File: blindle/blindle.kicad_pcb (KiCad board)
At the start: 2 copper layers, 8 parts, among them J1 CONN_5V, J2 CONN_8V, M1 74HC595, P1 pololua4988, P2 pololua4988

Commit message: Actualizo la huella del pololu
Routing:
- net GNDD: track 78.9 -> 77.3 mm
- net +8V: track 65.2 -> 66.8 mm
- net +5V: track 223.3 -> 224.5 mm
- net Net-(P2-Pad14): track 14.8 -> 14.0 mm
- net Net-(P2-Pad13): track 14.8 -> 14.0 mm
- net Net-(P2-Pad12): track 14.8 -> 14.0 mm
- net Net-(P2-Pad11): track 14.8 -> 14.0 mm
- net Net-(P1-Pad14): track 14.1 -> 13.3 mm
- net Net-(P1-Pad13): track 14.1 -> 13.3 mm
- net Net-(P1-Pad12): track 14.1 -> 13.3 mm
- net Net-(P1-Pad11): track 14.1 -> 13.3 mm
- net GND: track 267.7 -> 266.9 mm

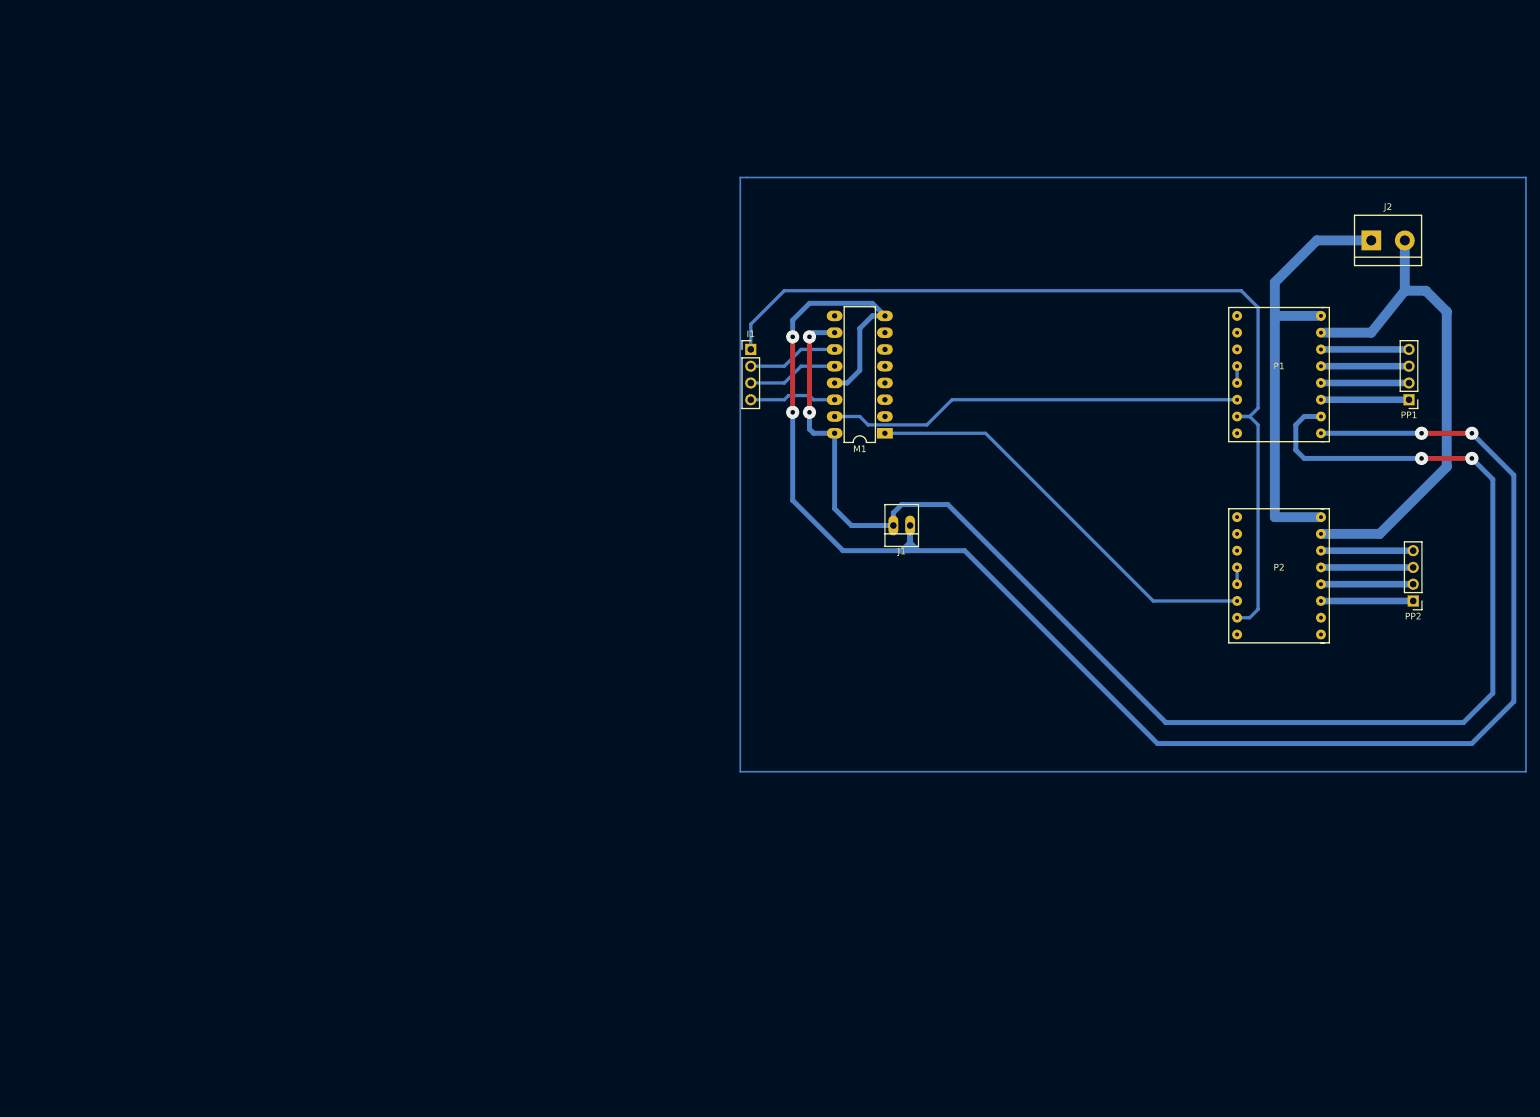
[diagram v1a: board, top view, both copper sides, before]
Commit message: Bug en plantilla pololu - Version 4 pololus
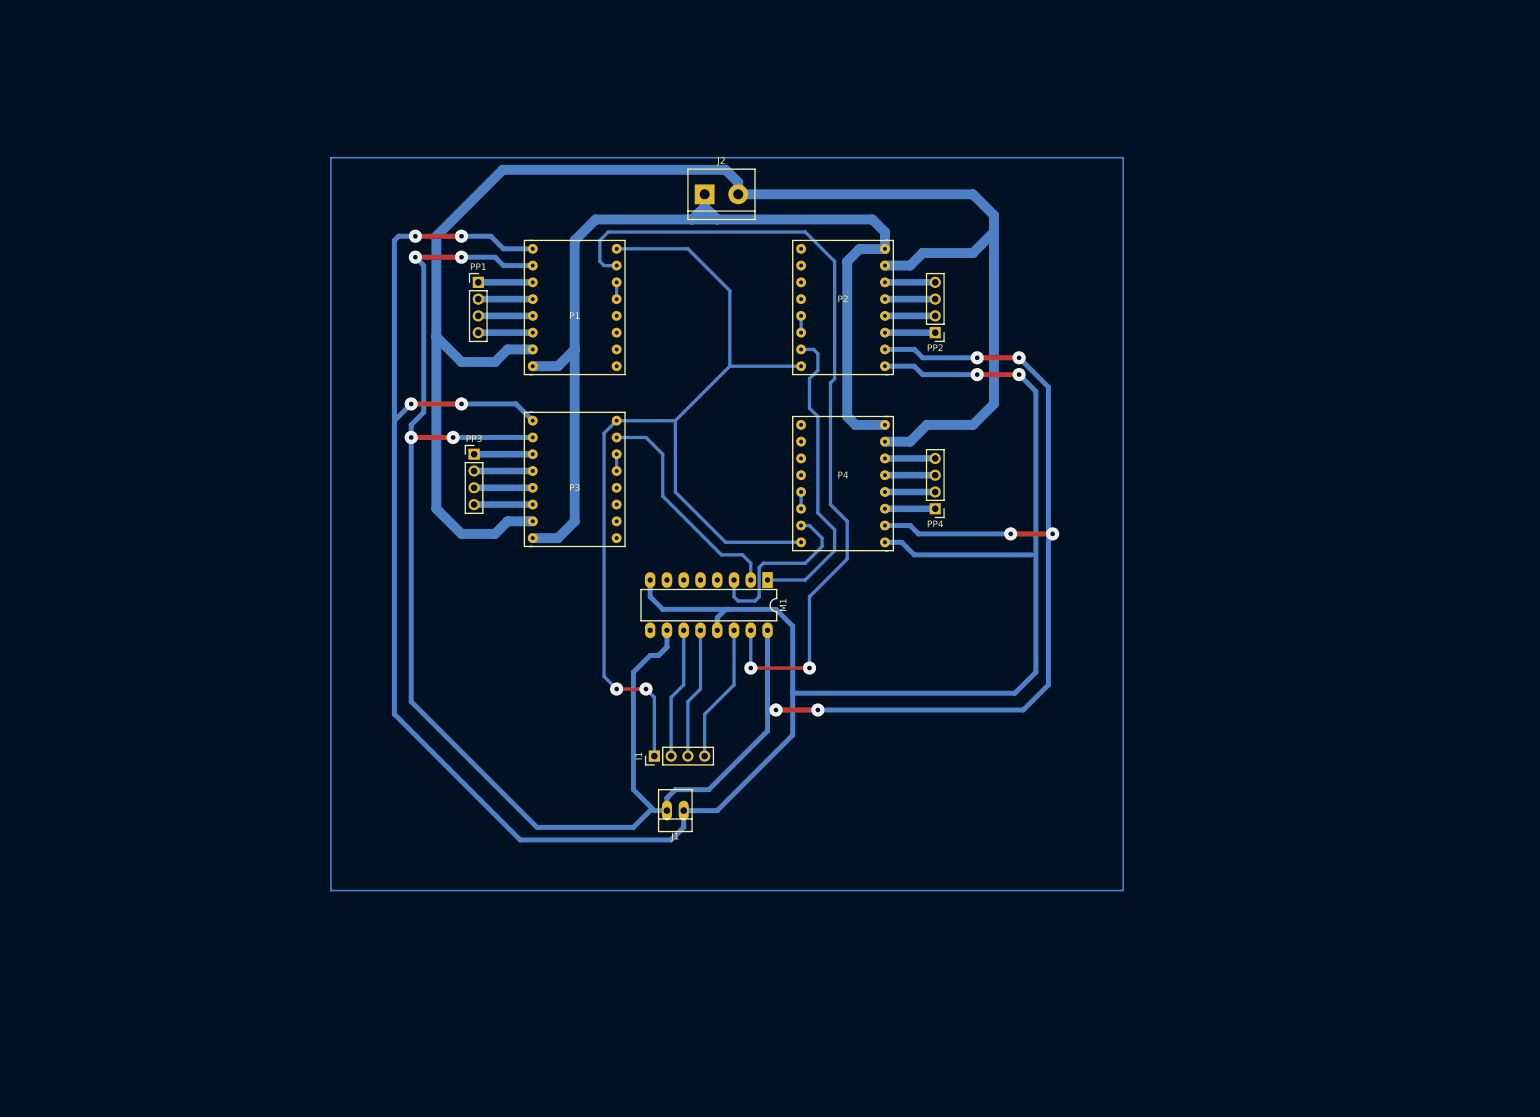
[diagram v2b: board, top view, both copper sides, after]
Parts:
- added P3: pololua4988, pololu:pololua4988, F.Cu at (128.3, 94.6)
- added P4: pololua4988, pololu:pololua4988, F.Cu at (156.2, 77.5)
- added PP3: CONN_MOTOR, Pin_Headers:Pin_Header_Straight_1x04_Pitch2.54mm, F.Cu at (106.7, 81.9)
- added PP4: CONN_MOTOR, Pin_Headers:Pin_Header_Straight_1x04_Pitch2.54mm, F.Cu at (176.5, 90.2)
- moved PP1 142.1 mm to (107.3, 55.9), turned to 0 degrees
- moved J2 101.2 mm to (141.6, 42.5)
- moved P1 94.3 mm to (128.3, 68.6), turned to 180 degrees
- moved PP2 83.0 mm to (176.5, 63.5)
- moved P2 77.5 mm to (156.2, 50.8)
- moved I1 63.3 mm to (134.0, 127.6), turned to 90 degrees
- moved J1 55.1 mm to (138.4, 135.9)
- moved M1 28.5 mm to (151.1, 101.0), turned to 270 degrees
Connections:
- I1 pad 1: Net-(I1-Pad1) -> dir
- P1 pad 4: sleep -> Net-(P1-Pad4)
- P1 pad 5: sleep -> Net-(P1-Pad5)
- P1 pad 6: Net-(M1-Pad15) -> Net-(P1-Pad5)
- P1 pad 7: Net-(I1-Pad1) -> Net-(M1-Pad15)
- P1 pad 8: (no net) -> dir
- P2 pad 5: Net-(P2-Pad4) -> Net-(P2-Pad5)
- P2 pad 6: Net-(M1-Pad1) -> Net-(P2-Pad5)
- P2 pad 7: Net-(I1-Pad1) -> Net-(M1-Pad1)
- P2 pad 8: (no net) -> dir
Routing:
- net GNDD: track 77.3 -> 233.8 mm
- net +5V: track 224.5 -> 378.7 mm, vias 4 -> 10
- net dir: track 0.00 -> 152.9 mm, vias 0 -> 2
- net Net-(I1-Pad1): track 138.1 -> 0.00 mm
- net GND: track 266.9 -> 368.1 mm, vias 4 -> 6
- net +8V: track 66.8 -> 152.5 mm
- net Net-(M1-Pad15): track 63.1 -> 123.8 mm, vias 0 -> 2
- net (no net): track 418.0 -> 462.0 mm
- net Net-(M1-Pad2): track 0.00 -> 34.5 mm
- net Net-(M1-Pad3): track 0.00 -> 27.4 mm
- net Net-(M1-Pad1): track 63.9 -> 46.8 mm
- net Net-(P3-Pad14): track 0.00 -> 8.89 mm
- net Net-(P3-Pad13): track 0.00 -> 8.89 mm
- net Net-(P3-Pad12): track 0.00 -> 8.89 mm
- net Net-(P3-Pad11): track 0.00 -> 8.89 mm
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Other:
- net class 8v: clearance 1 -> 0.5
- net class 8v-min: clearance 0.5 -> 0.2

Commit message: 8 pololu - En desarrollo
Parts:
- added I2: CONN_MULTI2, Pin_Headers:Pin_Header_Straight_1x04_Pitch2.54mm, F.Cu at (163.8, 153.7)
- added P5: pololua4988, pololu:pololua4988, F.Cu at (128.3, 100.3)
- added P6: pololua4988, pololu:pololua4988, F.Cu at (154.9, 83.8)
- added P7: pololua4988, pololu:pololua4988, F.Cu at (128.3, 127.0)
- added P8: pololua4988, pololu:pololua4988, F.Cu at (154.9, 109.2)
- added PP5: CONN_MOTOR, Pin_Headers:Pin_Header_Straight_1x04_Pitch2.54mm, F.Cu at (106.7, 87.6)
- added PP6: CONN_MOTOR, Pin_Headers:Pin_Header_Straight_1x04_Pitch2.54mm, F.Cu at (176.5, 96.5)
- added PP7: CONN_MOTOR, Pin_Headers:Pin_Header_Straight_1x04_Pitch2.54mm, F.Cu at (106.7, 114.3)
- added PP8: CONN_MOTOR, Pin_Headers:Pin_Header_Straight_1x04_Pitch2.54mm, F.Cu at (176.5, 121.9)
- moved M1 29.8 mm to (151.1, 130.8)
- moved J1 24.0 mm to (138.4, 159.9)
- moved I1 24.0 mm to (134.0, 151.6)
- moved PP3 20.3 mm to (106.7, 61.6)
- moved PP4 20.3 mm to (176.5, 69.8)
- moved J2 20.3 mm to (141.6, 22.2)
- moved P1 20.3 mm to (128.3, 48.3)
- moved P4 20.3 mm to (156.2, 57.1)
- moved PP1 20.3 mm to (107.3, 35.6)
- moved PP2 20.3 mm to (176.5, 43.2)
- moved P2 20.3 mm to (156.2, 30.5)
- moved P3 20.3 mm to (128.3, 74.3)
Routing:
- net (no net): track 462.0 -> 677.6 mm, vias 0 -> 2
- net GNDD: track 233.8 -> 411.7 mm
- net +8V: track 152.5 -> 278.6 mm
- net Net-(M1-Pad15): track 123.8 -> 0.00 mm, vias 2 -> 0
- net dir: track 152.9 -> 255.0 mm
- net GND: track 368.1 -> 424.0 mm, vias 6 -> 14
- net Net-(M1-Pad4): track 0.00 -> 55.0 mm
- net +5V: track 378.7 -> 427.4 mm, vias 10 -> 16
- net Net-(M1-Pad1): track 46.8 -> 0.00 mm
- net Net-(M1-Pad6): track 0.00 -> 27.0 mm
- net Net-(M1-Pad3): track 27.4 -> 5.23 mm
- net Net-(P8-Pad14): track 0.00 -> 8.89 mm
- net Net-(P8-Pad13): track 0.00 -> 8.89 mm
- net Net-(P8-Pad12): track 0.00 -> 8.89 mm
- net Net-(P8-Pad11): track 0.00 -> 8.89 mm
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
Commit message: pololu 8 - final v1 pcb
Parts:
- moved I2 5.68 mm to (161.3, 158.8), turned to 180 degrees
- moved M1 4.02 mm to (149.9, 134.6)
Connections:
- I2 pad 1: Net-(I1-Pad3) -> dir
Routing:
- net (no net): track 677.6 -> 539.5 mm, vias 2 -> 0
- net GND: track 424.0 -> 560.2 mm, vias 14 -> 20
- net Net-(M1-Pad15): track 0.00 -> 129.9 mm
- net Net-(M1-Pad1): track 0.00 -> 101.2 mm, vias 0 -> 2
- net Net-(M1-Pad3): track 5.23 -> 84.4 mm
- net +5V: track 427.4 -> 498.5 mm, vias 16 -> 18
- net Net-(M1-Pad2): track 42.7 -> 107.0 mm
- net Net-(M1-Pad5): track 0.00 -> 52.8 mm
- net dir: track 255.0 -> 302.4 mm, vias 2 -> 4
- net Net-(I2-Pad4): track 0.00 -> 38.3 mm
- net Net-(M1-Pad7): track 0.00 -> 28.2 mm, vias 0 -> 2
- net Net-(I1-Pad2): track 14.0 -> 38.7 mm
- net Net-(I1-Pad3): track 14.0 -> 33.5 mm
- net Net-(M1-Pad6): track 27.0 -> 35.1 mm
- net Net-(M1-Pad4): track 55.0 -> 59.0 mm
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
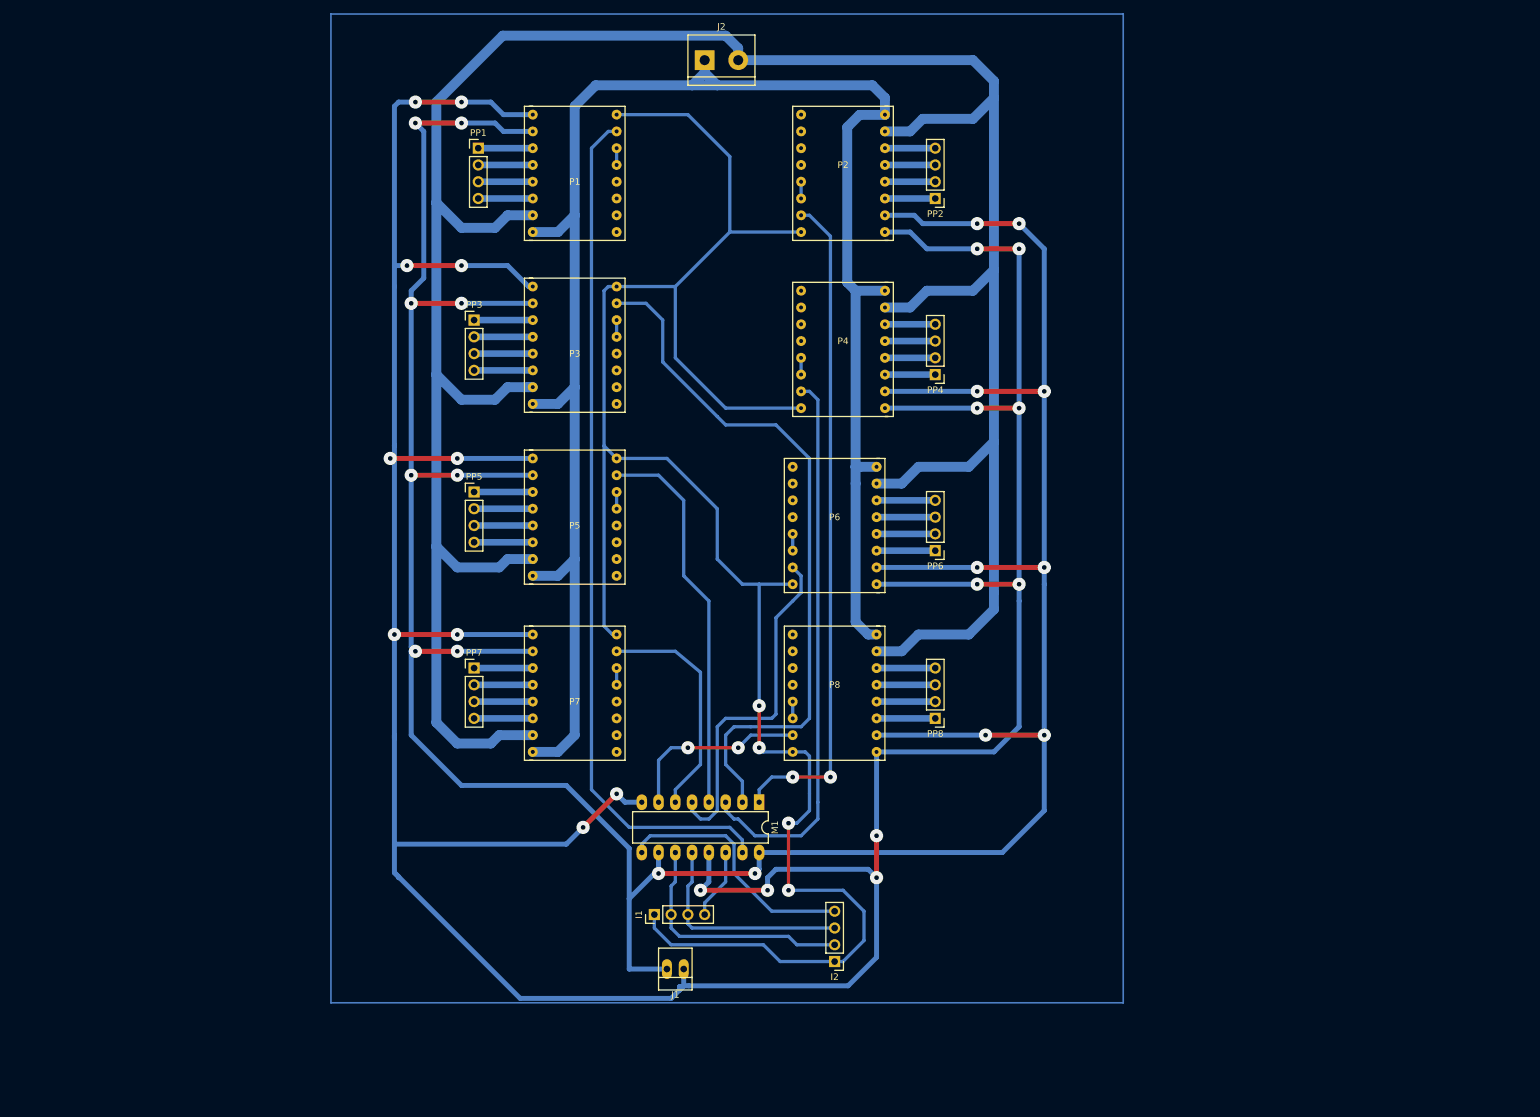
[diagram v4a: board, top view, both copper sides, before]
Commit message: Refinamiento de diseño pcb y footprint pololu
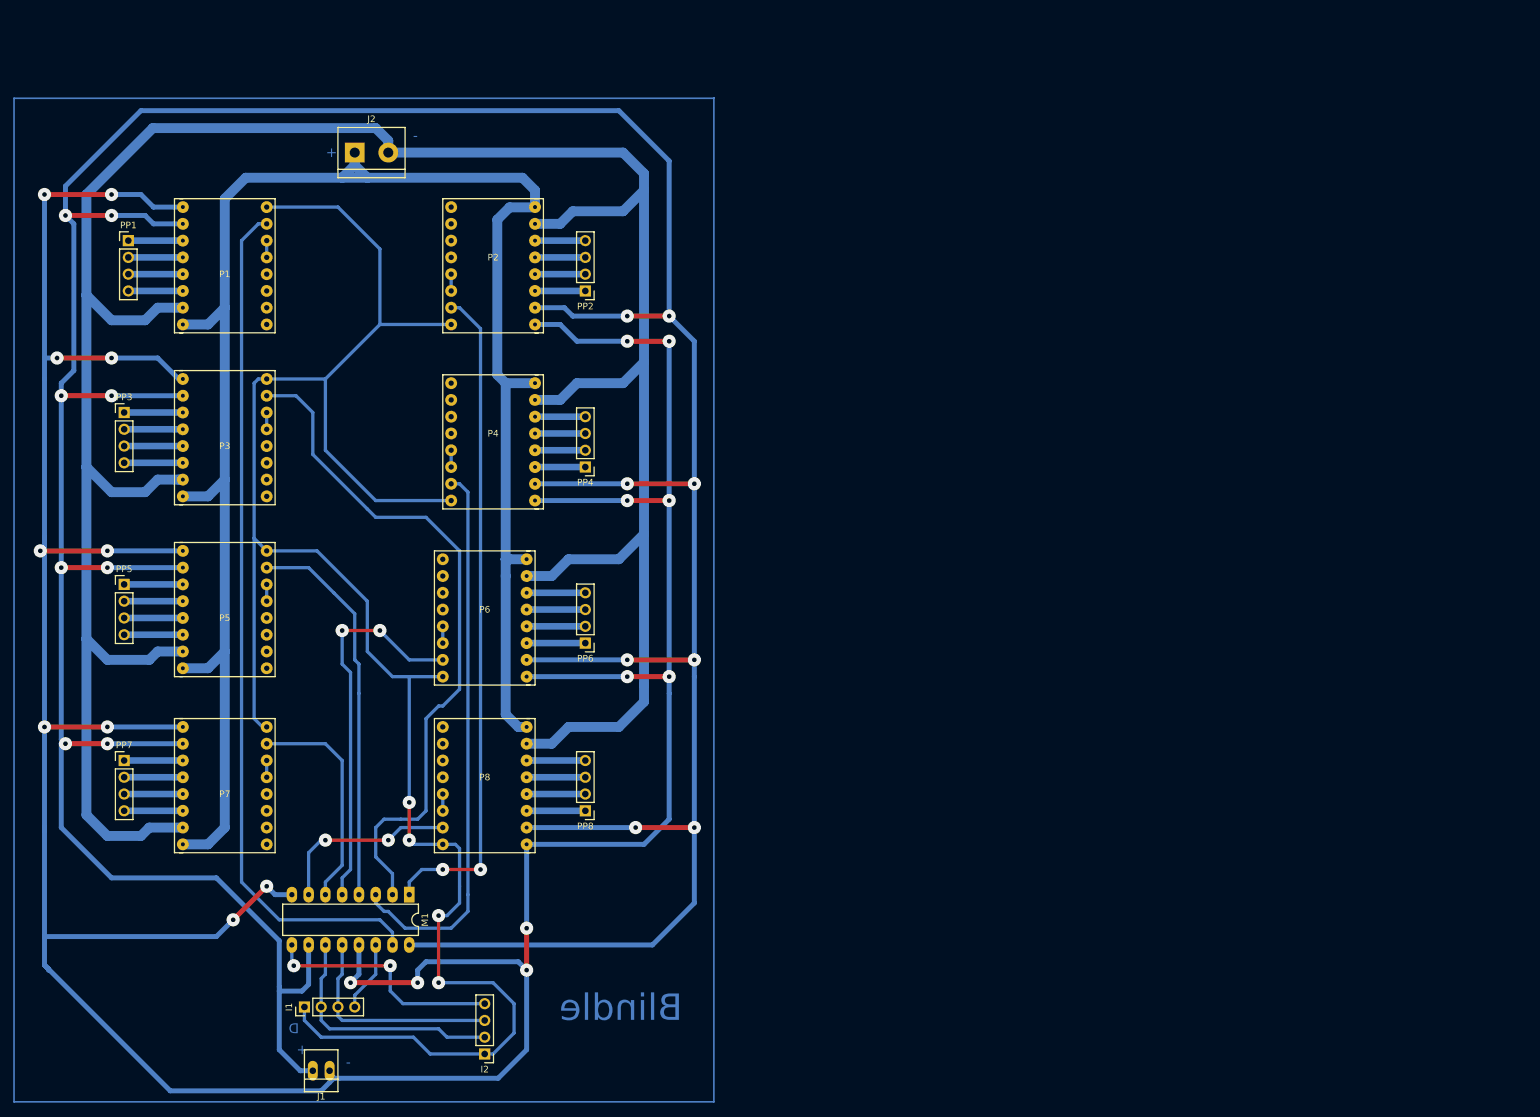
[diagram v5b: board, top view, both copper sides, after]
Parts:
- moved J1 55.8 mm to (84.8, 175.3)
- moved PP7 54.8 mm to (53.7, 128.3)
- moved I1 54.8 mm to (81.0, 165.6)
- moved M1 54.8 mm to (96.9, 148.6)
- moved P1 54.8 mm to (75.3, 62.3)
- moved P2 54.8 mm to (103.2, 44.5)
- moved P3 54.8 mm to (75.3, 88.3)
- moved P4 54.8 mm to (103.2, 71.2)
- moved P5 54.8 mm to (75.3, 114.3)
- moved P7 54.8 mm to (75.3, 141.0)
- moved PP3 54.8 mm to (53.7, 75.6)
- moved PP5 54.8 mm to (53.7, 101.6)
- moved P6 54.8 mm to (101.9, 97.8)
- moved P8 54.8 mm to (101.9, 123.2)
- moved PP1 54.8 mm to (54.3, 49.6)
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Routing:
- net +5V: track 498.5 -> 605.5 mm, vias 18 -> 16
- net (no net): track 539.5 -> 516.1 mm
- net Net-(M1-Pad5): track 52.8 -> 58.1 mm, vias 0 -> 2
- net Net-(M1-Pad2): track 107.0 -> 104.4 mm
- net Net-(I2-Pad4): track 38.3 -> 36.8 mm, vias 0 -> 2
- net Net-(M1-Pad6): track 35.1 -> 33.9 mm
- net GND: track 560.2 -> 559.0 mm
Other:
- board text added: "+"
- board text added: "-"
- board text added: "Blindle"
- board text added: "D"

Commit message: version de placa final
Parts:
- moved I1 119.4 mm to (200.4, 161.6)
- moved J1 119.4 mm to (204.2, 171.2)
- moved J2 119.4 mm to (208.0, 32.2)
- moved M1 119.4 mm to (216.2, 144.6)
- moved P1 119.4 mm to (194.7, 58.2)
- moved P2 119.4 mm to (222.6, 40.4)
- moved P3 119.4 mm to (194.7, 84.2)
- moved P4 119.4 mm to (222.6, 67.1)
- moved P5 119.4 mm to (194.7, 110.3)
- moved P7 119.4 mm to (194.7, 136.9)
- moved P6 119.4 mm to (221.3, 93.8)
- moved P8 119.4 mm to (221.3, 119.2)
- moved PP1 119.4 mm to (173.7, 45.5)
- moved PP2 119.4 mm to (242.9, 53.1)
- moved PP3 119.4 mm to (173.1, 71.5)
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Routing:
- net GND: track 559.0 -> 557.7 mm
